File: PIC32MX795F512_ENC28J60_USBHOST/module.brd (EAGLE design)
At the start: 83.2 x 68.6 mm, 75 parts, among them IC1 IC_USBLC6-2, IC2 LM1117IMPX-3.3, IC3 PIC32MX795F512, IC4 ENC28J60, T1 BC847, U1 USD-SOCKETUSD, X1 22-23-2021, X2 CRYSTALS-NOGND-CFPX-217, X3 KUSBVX, X4 22-23-2021, X5 22-23-2021, Y1 CRYSTAL-GROUNDEDSMD-5X3.2, Y2 CRYSTAL-GROUNDEDSMD-5X3.2

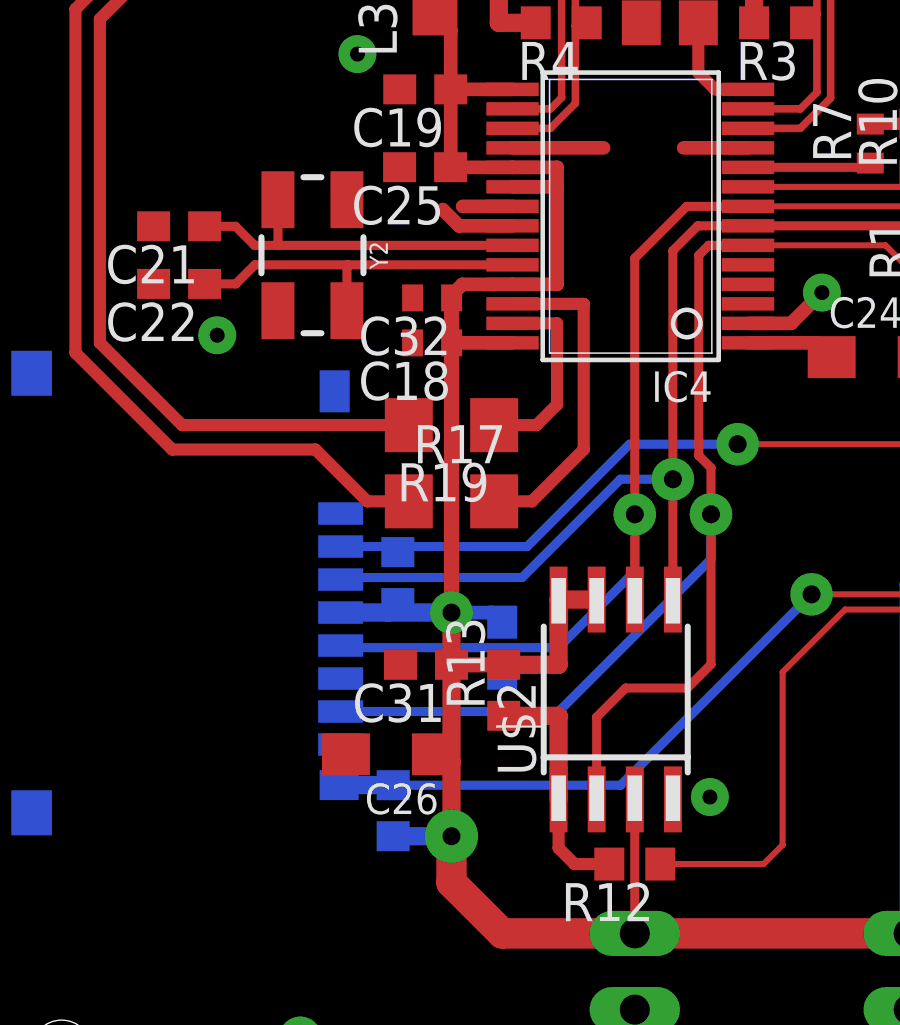
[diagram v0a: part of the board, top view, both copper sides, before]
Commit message: MISO pull-ups added
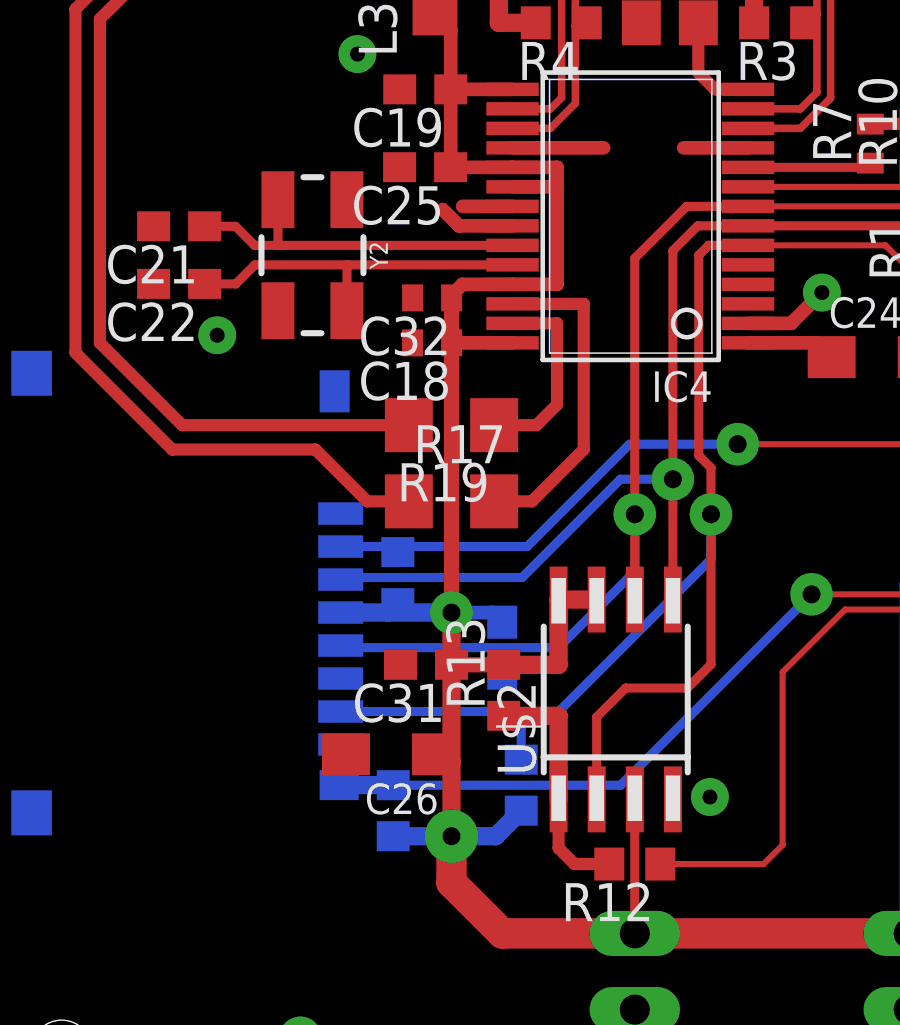
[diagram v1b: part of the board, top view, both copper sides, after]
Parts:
- added R20: (no value), rcl:R0603
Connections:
- net 3V_IN: now also R20.2
- net MISO: now also R20.1
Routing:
- net 3V_IN: track 225.2 -> 227.9 mm
- net MISO: track 60.8 -> 62.4 mm
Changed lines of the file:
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@@
 </element>
 <element name="R18" library="rcl" package="R0805" value="" x="43.18" y="47.625" rot="R270"/>
+<element name="R20" library="rcl" package="R0603" value="" x="20.32" y="13.8294" rot="MR270"/>
 </elements>
 <signals>
@@
 <wire x1="20.0288" y1="34.425" x2="21.5138" y2="34.425" width="0.4572" layer="1"/>
 <wire x1="21.5138" y1="34.425" x2="21.5138" y2="33.775" width="0.4572" layer="1"/>
-<wire x1="21.5138" y1="33.655" x2="21.5138" y2="30.525" width="0.4572" layer="1"/>
+<wire x1="21.5138" y1="33.775" x2="21.5138" y2="30.525" width="0.4572" layer="1"/>
 <wire x1="20.0288" y1="33.775" x2="21.5138" y2="33.775" width="0.4572" layer="1"/>
-<wire x1="21.5138" y1="33.775" x2="21.5138" y2="33.655" width="0.4572" layer="1"/>
+<contactref element="R20" pad="2"/>
+<wire x1="17.995" y1="12.1294" x2="19.47" y2="12.1294" width="0.6096" layer="16"/>
+<wire x1="19.47" y1="12.1294" x2="20.32" y2="12.9794" width="0.6096" layer="16"/>
 </signal>
 <signal name="3V">
@@
 <wire x1="26.6446" y1="22.86" x2="26.6446" y2="17.8562" width="0.3048" layer="1"/>
 <wire x1="26.6446" y1="17.8562" x2="25.8572" y2="17.0688" width="0.3048" layer="1"/>
-<wire x1="14.3" y1="16.285" x2="21.5682" y2="16.285" width="0.3048" layer="16"/>
+<wire x1="14.3" y1="16.285" x2="20.32" y2="16.285" width="0.3048" layer="16"/>
+<wire x1="20.32" y1="16.285" x2="21.5682" y2="16.285" width="0.3048" layer="16"/>
 <wire x1="26.6446" y1="21.59" x2="26.6446" y2="22.86" width="0.3048" layer="16"/>
 <wire x1="21.5682" y1="16.285" x2="26.6446" y2="21.3614" width="0.3048" layer="16"/>
@@
 <wire x1="34.8996" y1="30.2514" x2="34.8996" y2="30.9626" width="0.2032" layer="1"/>
 <wire x1="34.584640625" y1="31.277559375" x2="34.8996" y2="30.9626" width="0.2032" layer="1"/>
+<contactref element="R20" pad="1"/>
+<wire x1="20.32" y1="14.6794" x2="20.32" y2="16.285" width="0.3048" layer="16"/>
 </signal>
 <signal name="MOSI">
